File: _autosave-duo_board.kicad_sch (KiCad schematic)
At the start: 24 parts, among them J1 TRRS, J2 2171790001, J3 Conn_01x04_Pin, U1 STM32F103C8Tx, U3 AMS1117-3.3, Y1 16Mhz

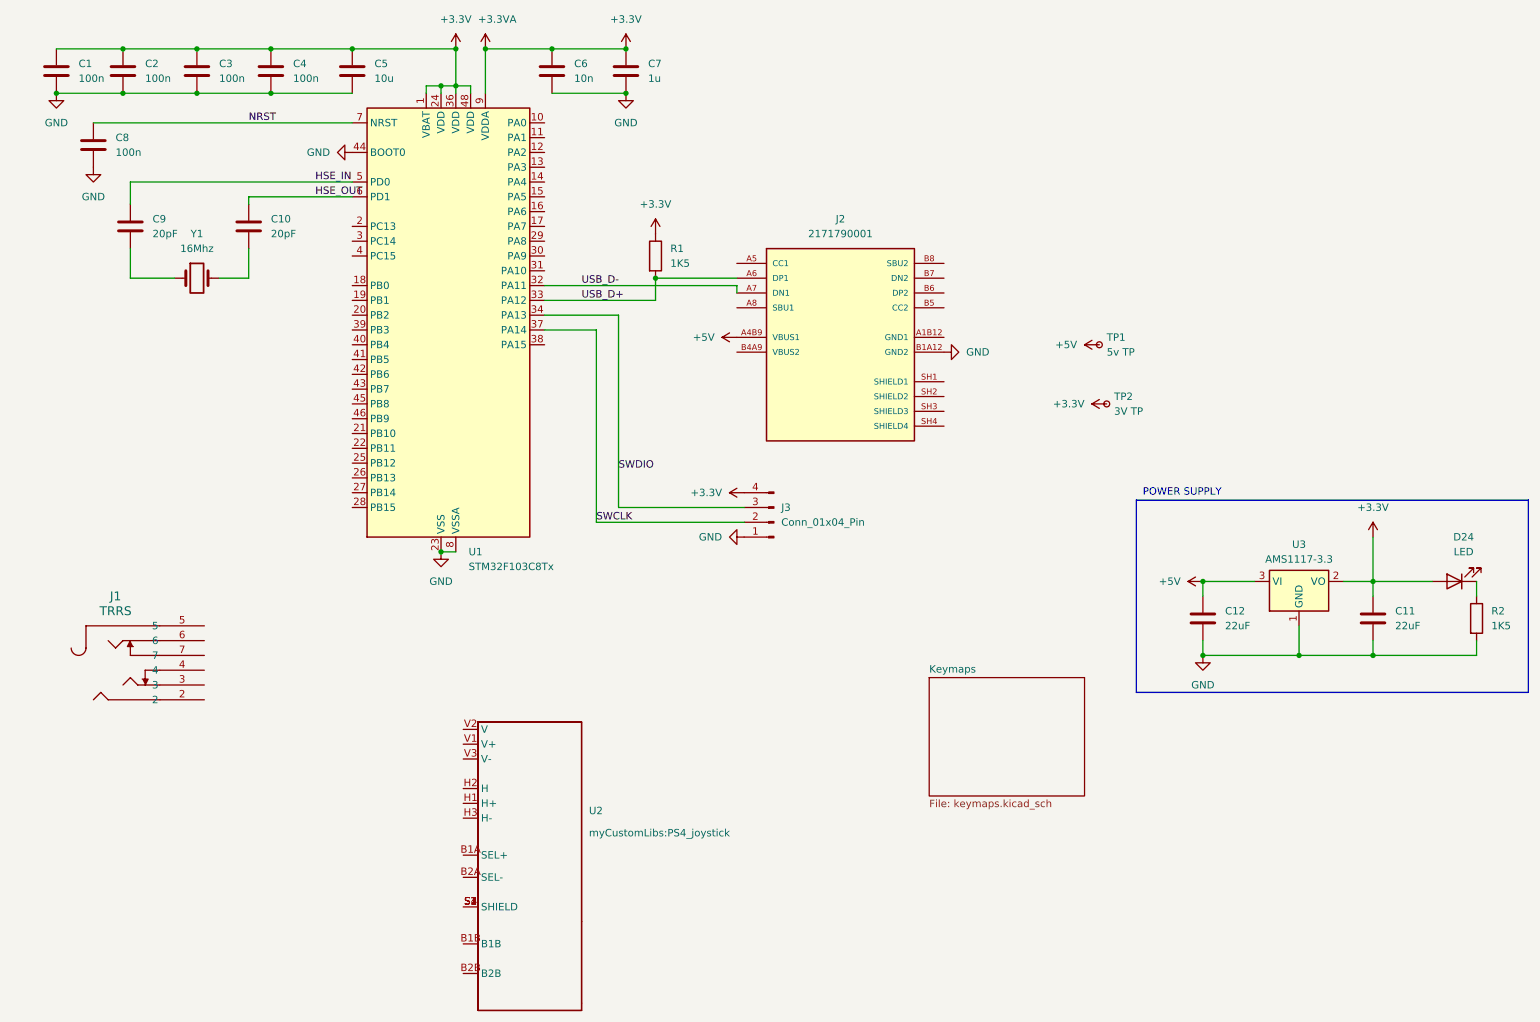
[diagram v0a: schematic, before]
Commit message: completed MCU power supply
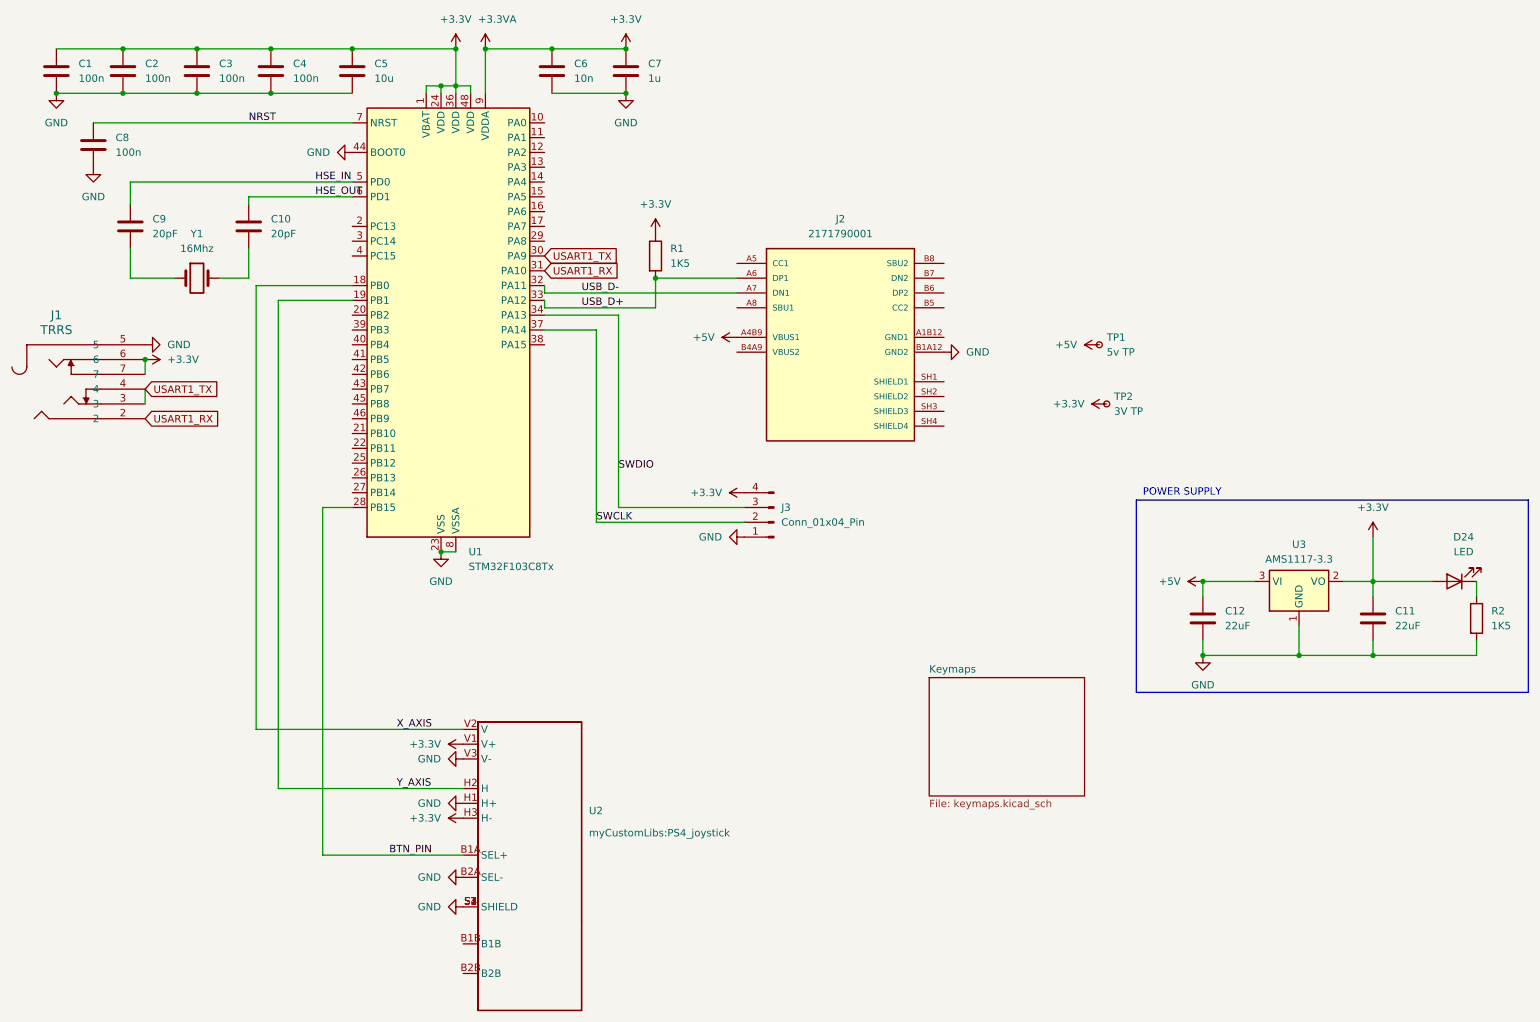
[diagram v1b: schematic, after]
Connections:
- net +3.3V: now also J1.6, J1.7, U2.H3 (H-), U2.V1 (V+)
- net GND: now also J1.5, U2.B2A (SEL-), U2.H1 (H+), U2.S1 (SHIELD), U2.S2 (SHIELD), U2.S3 (SHIELD), U2.S4 (SHIELD), U2.V3 (V-)
- net USART1_RX: now reaches J1.2
- net USART1_RX: now also U1.31 (PA10)
- net USART1_TX: now reaches J1.3
- net USART1_TX: now also J1.4, U1.30 (PA9)
- net X_AXIS: now reaches U1.18 (PB0)
- net X_AXIS: now also U2.V2 (V)
- net Y_AXIS: now reaches U1.19 (PB1)
- net Y_AXIS: now also U2.H2 (H)
- net BTN_PIN: now reaches U1.28 (PB15)
- net BTN_PIN: now also U2.B1A (SEL+)
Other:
- moved on the sheet: J1
